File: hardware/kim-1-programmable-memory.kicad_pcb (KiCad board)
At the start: 2 copper layers, 107.5 x 58.6 mm, 21 parts, among them J1 Conn_02x01, J3 EDGE_CONN, Q1 DMG2305UX, SW1 RESET, U1 74LVC541, U2 74LVC541, U3 74LVC245, U4 74LVC1G04, U6 74LVC1G38, U7 74LVC1G27, U8 PicoW

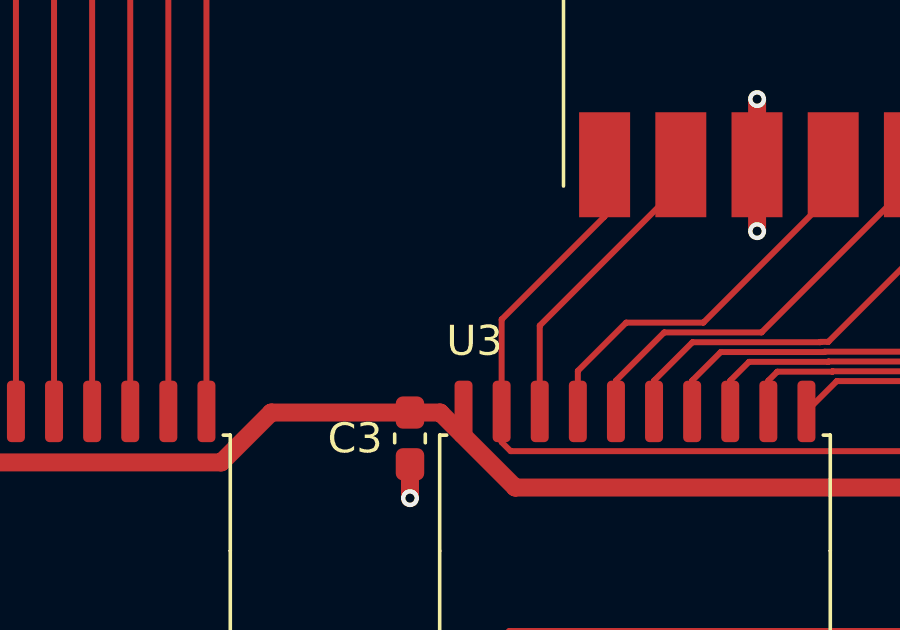
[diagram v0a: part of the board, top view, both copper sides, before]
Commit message: Add pull-up resistor to OE
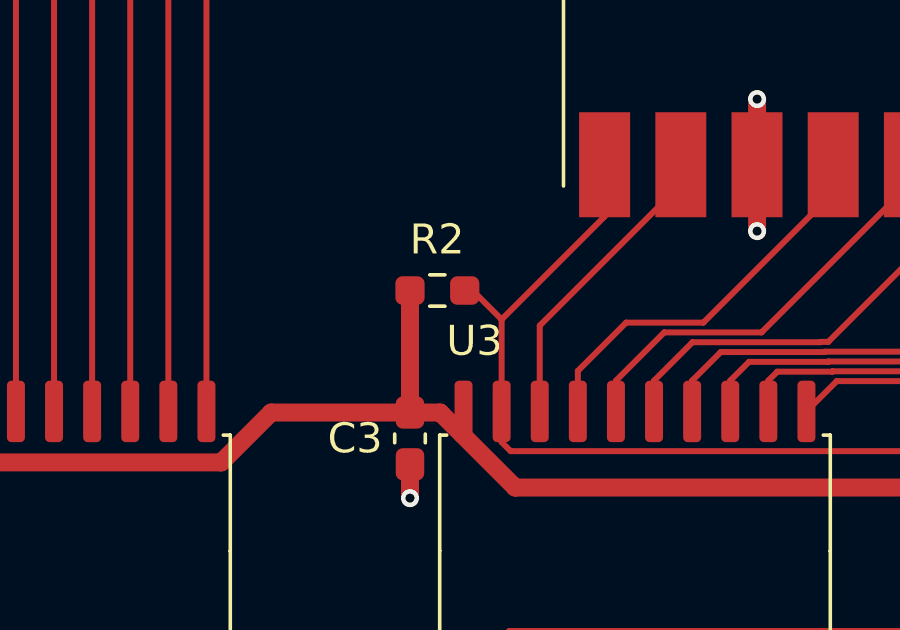
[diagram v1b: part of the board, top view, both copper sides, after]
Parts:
- added R2: 3K3, Resistor_SMD:R_0603_1608Metric_Pad0.98x0.95mm_HandSolder, F.Cu at (103.1, 136.7)
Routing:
- net +3.3V: track 102.3 -> 106.3 mm
- net /~{CE}: track 47.3 -> 48.9 mm
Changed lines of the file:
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@@
   (net 77 "unconnected-(J3-~{Ø2}-PadY)")
   (net 78 "/~{R}{slash}W'")
+  (footprint "Resistor_SMD:R_0603_1608Metric_Pad0.98x0.95mm_HandSolder" (layer "F.Cu")
+    (at 103.0625 136.7 180)
+    (descr "Resistor SMD 0603 (1608 Metric), square (rectangular) end terminal, IPC_7351 nominal with elongated pad for handsoldering. (Body size source: IPC-SM-782 page 72, https://www.pcb-3d.com/wordpress/wp-content/uploads/ipc-sm-782a_amendment_1_and_2.pdf), generated with kicad-footprint-generator")
+    (tags "resistor handsolder")
+    (property "Sheetfile" "kim-1-programmable-memory.kicad_sch")
+    (property "Sheetname" "")
+    (property "ki_description" "Resistor, small US symbol")
+    (property "ki_keywords" "r resistor")
+    (attr smd)
+    (fp_text reference "R2" (at 0.0125 1.7) (layer "F.SilkS")
+        (effects (font (size 1 1) (thickness 0.15)))
+    )
+    (fp_text value "3K3" (at 0 1.43) (layer "F.Fab")
+        (effects (font (size 1 1) (thickness 0.15)))
+    )
+    (fp_text user "${REFERENCE}" (at 0 0) (layer "F.Fab")
+        (effects (font (size 0.4 0.4) (thickness 0.06)))
+    )
+    (fp_line (start -0.254724 -0.5225) (end 0.254724 -0.5225)
+      (stroke (width 0.12) (type solid)) (layer "F.SilkS"))
+    (fp_line (start -0.254724 0.5225) (end 0.254724 0.5225)
+      (stroke (width 0.12) (type solid)) (layer "F.SilkS"))
+    (fp_line (start -1.65 -0.73) (end 1.65 -0.73)
+      (stroke (width 0.05) (type solid)) (layer "F.CrtYd"))
+    (fp_line (start -1.65 0.73) (end -1.65 -0.73)
+      (stroke (width 0.05) (type solid)) (layer "F.CrtYd"))
+    (fp_line (start 1.65 -0.73) (end 1.65 0.73)
+      (stroke (width 0.05) (type solid)) (layer "F.CrtYd"))
+    (fp_line (start 1.65 0.73) (end -1.65 0.73)
+      (stroke (width 0.05) (type solid)) (layer "F.CrtYd"))
+    (fp_line (start -0.8 -0.4125) (end 0.8 -0.4125)
+      (stroke (width 0.1) (type solid)) (layer "F.Fab"))
+    (fp_line (start -0.8 0.4125) (end -0.8 -0.4125)
+      (stroke (width 0.1) (type solid)) (layer "F.Fab"))
+    (fp_line (start 0.8 -0.4125) (end 0.8 0.4125)
+      (stroke (width 0.1) (type solid)) (layer "F.Fab"))
+    (fp_line (start 0.8 0.4125) (end -0.8 0.4125)
+      (stroke (width 0.1) (type solid)) (layer "F.Fab"))
+    (pad "1" smd roundrect (at -0.9125 0 180) (size 0.975 0.95) (layers "F.Cu" "F.Paste" "F.Mask") (roundrect_rratio 0.25)
+      (net 28 "/~{CE}") (pintype "passive"))
+    (pad "2" smd roundrect (at 0.9125 0 180) (size 0.975 0.95) (layers "F.Cu" "F.Paste" "F.Mask") (roundrect_rratio 0.25)
+      (net 35 "+3.3V") (pintype "passive"))
+    (model "${KICAD6_3DMODEL_DIR}/Resistor_SMD.3dshapes/R_0603_1608Metric.wrl"
+      (offset (xyz 0 0 0))
+      (scale (xyz 1 1 1))
+      (rotate (xyz 0 0 0))
+    )
+  )
   (footprint "Capacitor_SMD:C_0603_1608Metric_Pad1.08x0.95mm_HandSolder" (layer "F.Cu")
     (at 102.15 141.63 90)
@@
   (segment (start 105.505001 142.055) (end 132.355 142.055) (width 0.2) (layer "F.Cu") (net 28))
   (segment (start 105.205 141.754999) (end 105.505001 142.055) (width 0.2) (layer "F.Cu") (net 28))
+  (segment (start 105.205 137.665) (end 104.24 136.7) (width 0.2) (layer "F.Cu") (net 28))
   (segment (start 105.205 140.73) (end 105.205 141.754999) (width 0.2) (layer "F.Cu") (net 28))
   (segment (start 105.205 137.665) (end 108.6375 134.2325) (width 0.2) (layer "F.Cu") (net 28))
   (segment (start 138.96 141.49) (end 139.78 141.49) (width 0.2) (layer "F.Cu") (net 28))
+  (segment (start 104.24 136.7) (end 103.975 136.7) (width 0.2) (layer "F.Cu") (net 28))
   (segment (start 105.205 140.73) (end 105.205 137.665) (width 0.2) (layer "F.Cu") (net 28))
   (segment (start 156.69 131.815) (end 156.8975 131.6075) (width 0.6) (layer "F.Cu") (net 31))
@@
   (segment (start 95.860882 142.43) (end 84.84 142.43) (width 0.6) (layer "F.Cu") (net 35))
   (segment (start 135.75 143.27) (end 135.75 141.445) (width 0.6) (layer "F.Cu") (net 35))
+  (segment (start 102.15 140.7675) (end 102.15 136.7) (width 0.6) (layer "F.Cu") (net 35))
   (segment (start 144.3175 140.54) (end 144.3175 137.82) (width 0.6) (layer "F.Cu") (net 35))
   (segment (start 63.1475 140.7675) (end 62.259552 140.7675) (width 0.6) (layer "F.Cu") (net 35))

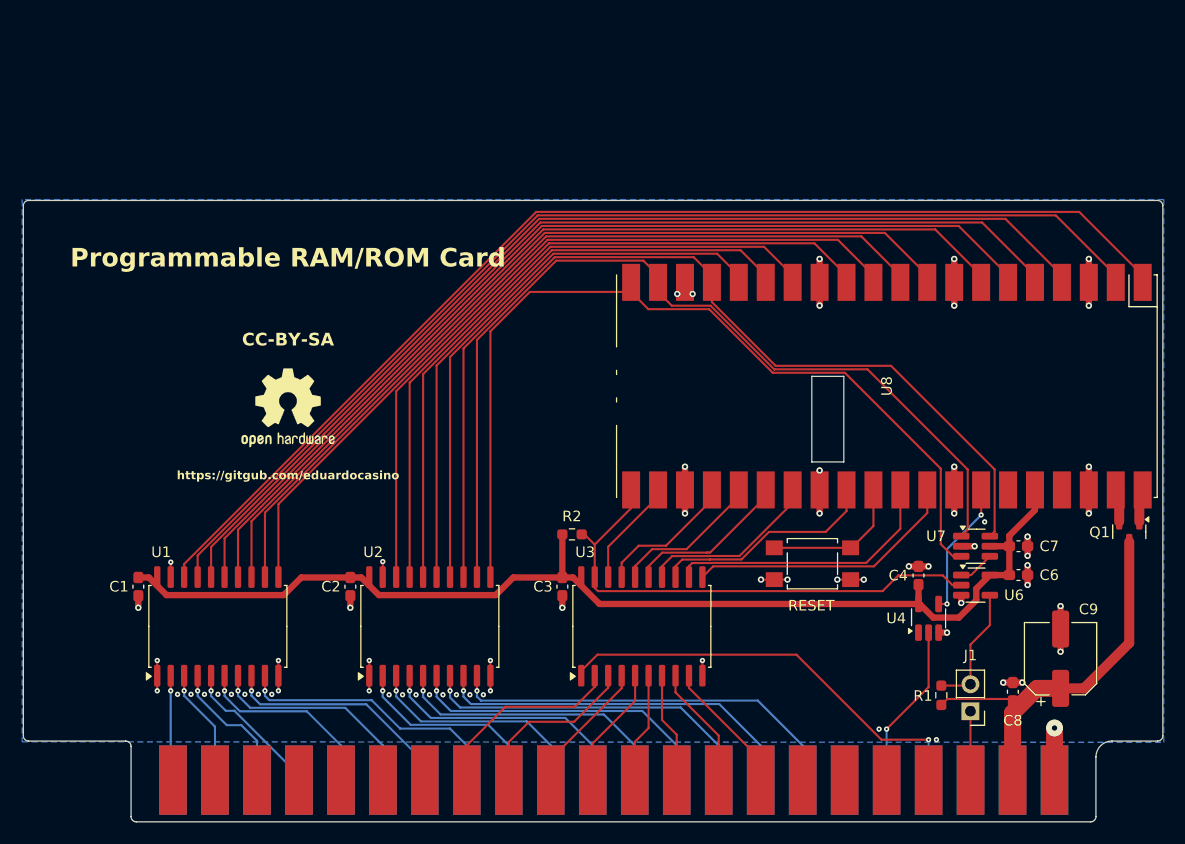
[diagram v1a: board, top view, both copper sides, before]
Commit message: New board design usign the RAMRW line
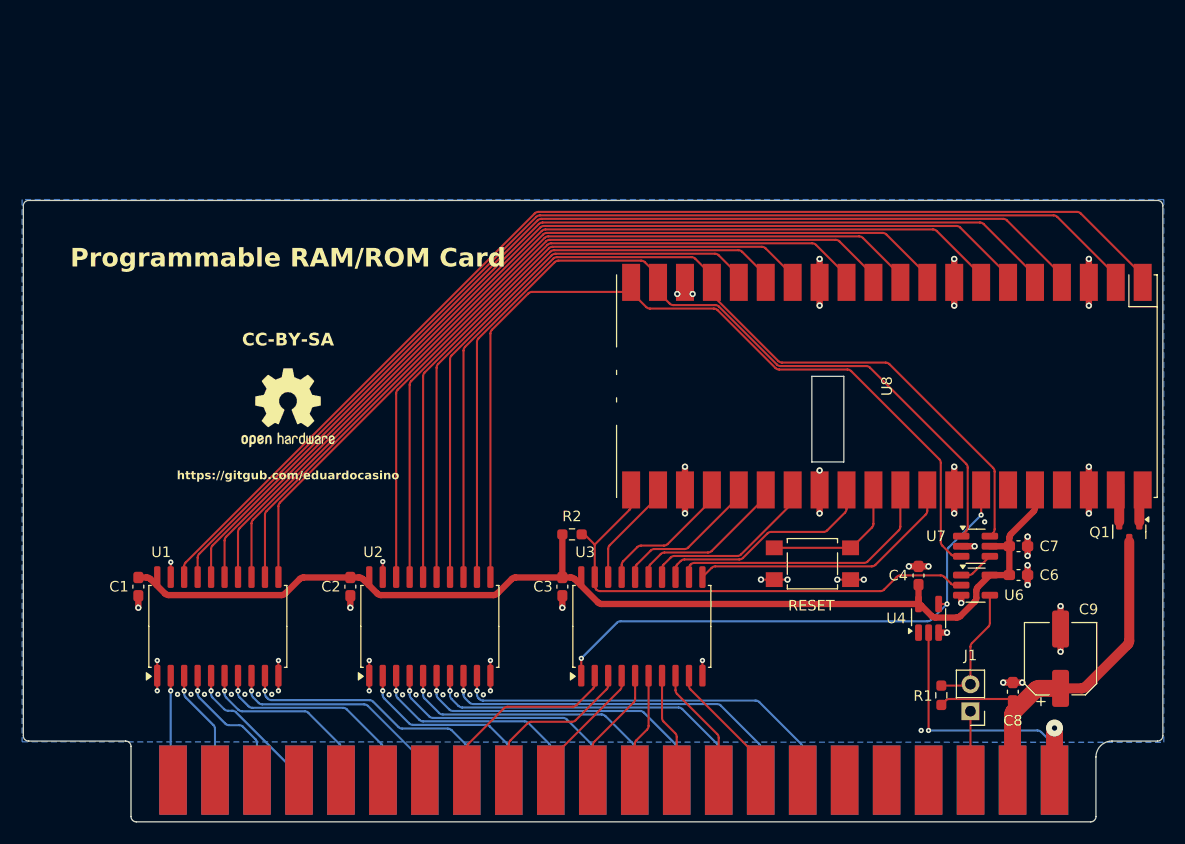
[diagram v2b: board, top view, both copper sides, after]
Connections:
- J3 pad V: /R/~{W} -> unconnected-(J3-R/~{W}-PadV)
- J3 pad W: /~{R}/W -> unconnected-(J3-~{R}/W-PadW)
- J3 pad Z: unconnected-(J3-RAMRW-PadZ) -> /RAMR~{W}
- U3 pad 1: /~{R}/W -> /RAM~{R}W
- U4 pad 2: /R/~{W} -> /RAMR~{W}
- U4 pad 4: /~{R}/W' -> /RAM~{R}W
- U8 pad 34: /~{R}/W' -> /RAM~{R}W
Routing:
- net /RAM~{R}W: track 0.00 -> 52.3 mm, vias 0 -> 3
- net /~{R}/W: track 41.0 -> 0.00 mm, vias 1 -> 0
- net /RAMR~{W}: track 0.00 -> 24.9 mm, vias 0 -> 1
- net /R/~{W}: track 15.6 -> 0.00 mm, vias 1 -> 0
- net /~{R}/W': track 14.2 -> 0.00 mm, vias 2 -> 0
- net /A13: track 89.9 -> 89.3 mm
- net GND: vias 67 -> 66

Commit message: New board design
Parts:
- removed the C4 at (135.8, 140.6)
- removed the U4 at (136.7, 144.6)
- added C1: 100nF, Capacitor_SMD:C_0603_1608Metric_Pad1.08x0.95mm_HandSolder, F.Cu at (121.7, 145.1)
- added C10: 10uF, Capacitor_SMD:C_0603_1608Metric_Pad1.08x0.95mm_HandSolder, F.Cu at (88.8, 105.8)
- added C11: 100nF, Capacitor_SMD:C_0603_1608Metric_Pad1.08x0.95mm_HandSolder, F.Cu at (88.8, 107.2)
- added C7: 100nF, Capacitor_SMD:C_0603_1608Metric_Pad1.08x0.95mm_HandSolder, F.Cu at (134.4, 104.8)
- added D1: HDD, LED_SMD:LED_0603_1608Metric_Pad1.05x0.95mm_HandSolder, F.Cu at (103.4, 91.9)
- added J3: VGA, Connector_Dsub:DSUB-15-HD_Female_Horizontal_P2.29x1.98mm_EdgePinOffset3.03mm_Housed_MountingHolesOffset4.94mm, F.Cu at (137.2, 95.8)
- added J4: VIdeo Out, CUI_Devices:CUI_RCJ-014, F.Cu at (116.0, 89.9)
- added J5: Micro_SD_Card_Det1, Micro-SD:SD_Card_Holder_SMD_WQ21801-B2180-7F, F.Cu at (88.7, 103.5)
- added R10: 40R, Resistor_SMD:R_0603_1608Metric_Pad0.98x0.95mm_HandSolder, F.Cu at (116.3, 136.1)
- added R11: 40R, Resistor_SMD:R_0603_1608Metric_Pad0.98x0.95mm_HandSolder, F.Cu at (93.0, 106.7)
- added R12: 470R, Resistor_SMD:R_0603_1608Metric_Pad0.98x0.95mm_HandSolder, F.Cu at (121.5, 101.7)
- added R13: 270R, Resistor_SMD:R_0603_1608Metric_Pad0.98x0.95mm_HandSolder, F.Cu at (121.5, 104.4)
- added R14: 270R, Resistor_SMD:R_0603_1608Metric_Pad0.98x0.95mm_HandSolder, F.Cu at (135.5, 98.9)
- added R15: 270R, Resistor_SMD:R_0603_1608Metric_Pad0.98x0.95mm_HandSolder, F.Cu at (135.5, 100.4)
- added R16: 270R, Resistor_SMD:R_0603_1608Metric_Pad0.98x0.95mm_HandSolder, F.Cu at (135.5, 101.9)
- added R17: 47R, Resistor_SMD:R_0603_1608Metric_Pad0.98x0.95mm_HandSolder, F.Cu at (135.5, 103.3)
- added R18: 47R, Resistor_SMD:R_0603_1608Metric_Pad0.98x0.95mm_HandSolder, F.Cu at (132.9, 143.1)
- added R19: 100R, Resistor_SMD:R_0603_1608Metric_Pad0.98x0.95mm_HandSolder, F.Cu at (103.4, 95.1)
- added R3: 5K1, Resistor_SMD:R_0603_1608Metric_Pad0.98x0.95mm_HandSolder, F.Cu at (122.6, 148.2)
- added R4: 10K, Resistor_SMD:R_0603_1608Metric_Pad0.98x0.95mm_HandSolder, F.Cu at (88.8, 108.7)
- added R7: 10K, Resistor_SMD:R_0603_1608Metric_Pad0.98x0.95mm_HandSolder, F.Cu at (108.6, 136.1)
- added R8: 40R, Resistor_SMD:R_0603_1608Metric_Pad0.98x0.95mm_HandSolder, F.Cu at (111.2, 136.1)
- added R9: 40R, Resistor_SMD:R_0603_1608Metric_Pad0.98x0.95mm_HandSolder, F.Cu at (118.8, 136.1)
- added U1: LVC04, Package_SO:SOIC-14_3.9x8.7mm_P1.27mm, F.Cu at (128.2, 147.6)
- added U7: LVC04, Package_SO:SOIC-14_3.9x8.7mm_P1.27mm, F.Cu at (128.2, 101.9)
- C8: footprint Capacitor_SMD:C_0603_1608Metric_Pad1.08x0.95mm_HandSolder -> Capacitor_SMD:C_0805_2012Metric_Pad1.18x1.45mm_HandSolder
- R2: value 3K3 -> 5K1
- moved R2 21.2 mm to (118.2, 151.5), turned to 0 degrees
- moved C5 18.2 mm to (118.3, 150.0), turned to 180 degrees
- moved REF** 2.66 mm to (78.3, 126.4)
- moved SW1 2.52 mm to (127.9, 138.2)
- moved C3 1.81 mm to (61.8, 139.9), turned to -90 degrees
- moved C4 1.77 mm to (82.0, 139.9), turned to -90 degrees
- moved C2 1.49 mm to (145.2, 142.0)
- moved U2 1.49 mm to (141.1, 143.0)
- turned U5 to -90 degrees
- renumbered C6 to C2, C1 to C3, C2 to C4, C3 to C5, C7 to C6, J3 to J2, U6 to U2, U1 to U3, U2 to U4, U3 to U5, U7 to U6
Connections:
- J2 pad W: unconnected-(J3-~{R}/W-PadW) -> /~{R}/W
- J2 pad Y: unconnected-(J3-~{Ø2}-PadY) -> /~{Ø2}
- J2 pad Z: /RAMR~{W} -> unconnected-(J2-RAMRW-PadZ)
- U3 pad 11: /A7 -> /AD7
- U3 pad 12: /A6 -> /AD6
- U3 pad 13: /A5 -> /AD5
- U3 pad 14: /A4 -> /AD4
- U3 pad 15: /A3 -> /AD3
- U3 pad 16: /A2 -> /AD2
- U3 pad 17: /A1 -> /AD1
- U3 pad 18: /A0 -> /AD0
- U4 pad 1: GND -> Net-(U4-G1)
- U5 pad 1: /RAM~{R}W -> /R/~{W}
- U5 pad 11: /D0 -> /DB7
- U5 pad 12: /D1 -> /DB6
- U5 pad 13: /D2 -> /DB5
- U5 pad 14: /D3 -> /DB4
- U5 pad 15: /D4 -> /DB3
- U5 pad 16: /D5 -> /DB2
- U5 pad 17: /D6 -> /DB1
- U5 pad 18: /D7 -> /DB0
- U5 pad 2: /DB7 -> /AD0
- U5 pad 3: /DB6 -> /AD1
- U5 pad 4: /DB5 -> /AD2
- U5 pad 5: /DB4 -> /AD3
- U5 pad 6: /DB3 -> /AD4
- U5 pad 7: /DB2 -> /AD5
- U5 pad 8: /DB1 -> /AD6
- U5 pad 9: /DB0 -> /AD7
- U8 pad 1: /A0 -> /AD0
- U8 pad 10: /A7 -> /AD7
- U8 pad 2: /A1 -> /AD1
- U8 pad 21: /~{CE} -> /RX
- U8 pad 22: /D7 -> /CSn
- U8 pad 24: /D6 -> /SCK
- U8 pad 25: /D5 -> /TX
- U8 pad 26: /D4 -> /~{CE}
- U8 pad 27: /D3 -> /R/~{W}
- U8 pad 29: /D2 -> /Ø2
- U8 pad 31: /D1 -> /VSYNC
- U8 pad 32: /D0 -> /HSYNC
- U8 pad 34: /RAM~{R}W -> /VIDEO
- U8 pad 4: /A2 -> /AD2
- U8 pad 5: /A3 -> /AD3
- U8 pad 6: /A4 -> /AD4
- U8 pad 7: /A5 -> /AD5
- U8 pad 9: /A6 -> /AD6
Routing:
- net /AD0: track 0.00 -> 161.7 mm
- net /AD1: track 0.00 -> 155.6 mm
- net /AD2: track 0.00 -> 146.3 mm
- net /AD3: track 0.00 -> 140.1 mm
- net +3.3V: track 105.9 -> 244.3 mm, vias 0 -> 8
- net /AD4: track 0.00 -> 133.2 mm
- net /AD5: track 0.00 -> 127.0 mm
- net /AD6: track 0.00 -> 118.3 mm
- net /AD7: track 0.00 -> 111.8 mm
- net /A0: track 109.4 -> 0.00 mm
- net /A1: track 105.7 -> 0.00 mm
- net /A2: track 99.6 -> 0.00 mm
- net /A3: track 96.0 -> 0.00 mm
- net /A4: track 92.4 -> 0.00 mm
- net /A5: track 88.8 -> 0.00 mm
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- added copper zone on In1.Cu, net GND
- added copper zone on In2.Cu, net GND
- removed copper zone on B.Cu, net GND
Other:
- board size 107.5 x 58.6 mm -> 107.5 x 75.4 mm
- copper layers 2 -> 4

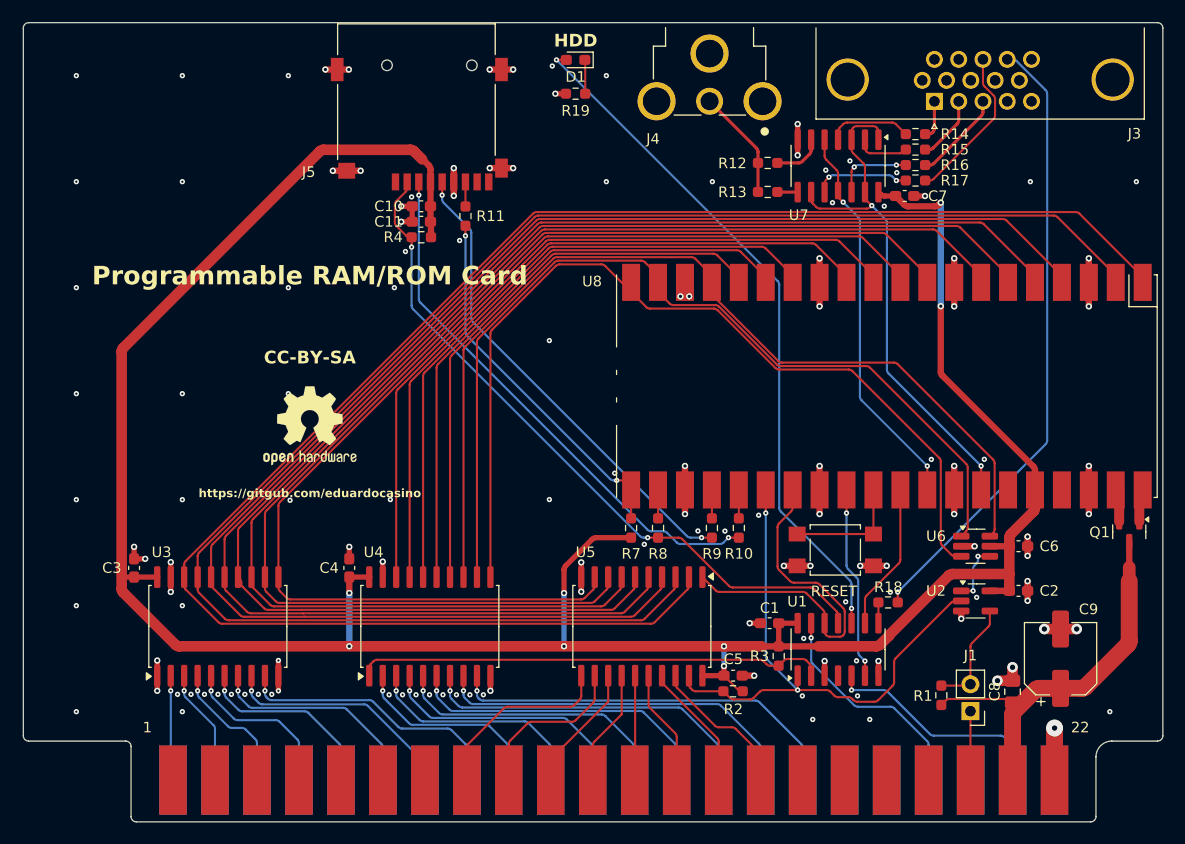
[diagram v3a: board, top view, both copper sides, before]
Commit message: Add LCSC parts and correct video tracks impedance
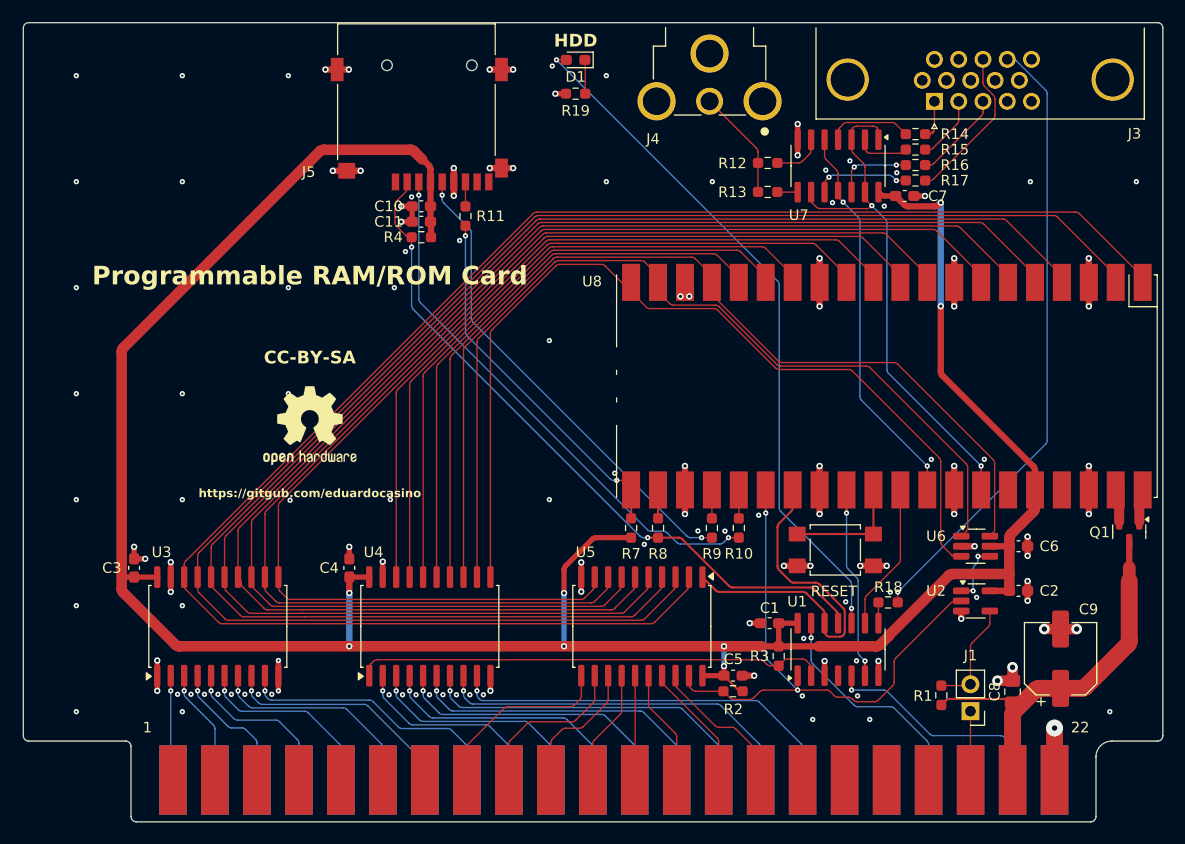
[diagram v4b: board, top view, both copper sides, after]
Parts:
- R2, R3: value 5K1 -> 3K3
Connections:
- net Net-(J3-Pad1) renamed /RED
- net Net-(J3-Pad2) renamed /GREEN
- net Net-(J3-Pad3) renamed /BLUE
- net Net-(J4-In) renamed /COMPOSITE
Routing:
- net /DB5: track 12.1 -> 13.0 mm
